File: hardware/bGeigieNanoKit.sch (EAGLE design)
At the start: 4 parts

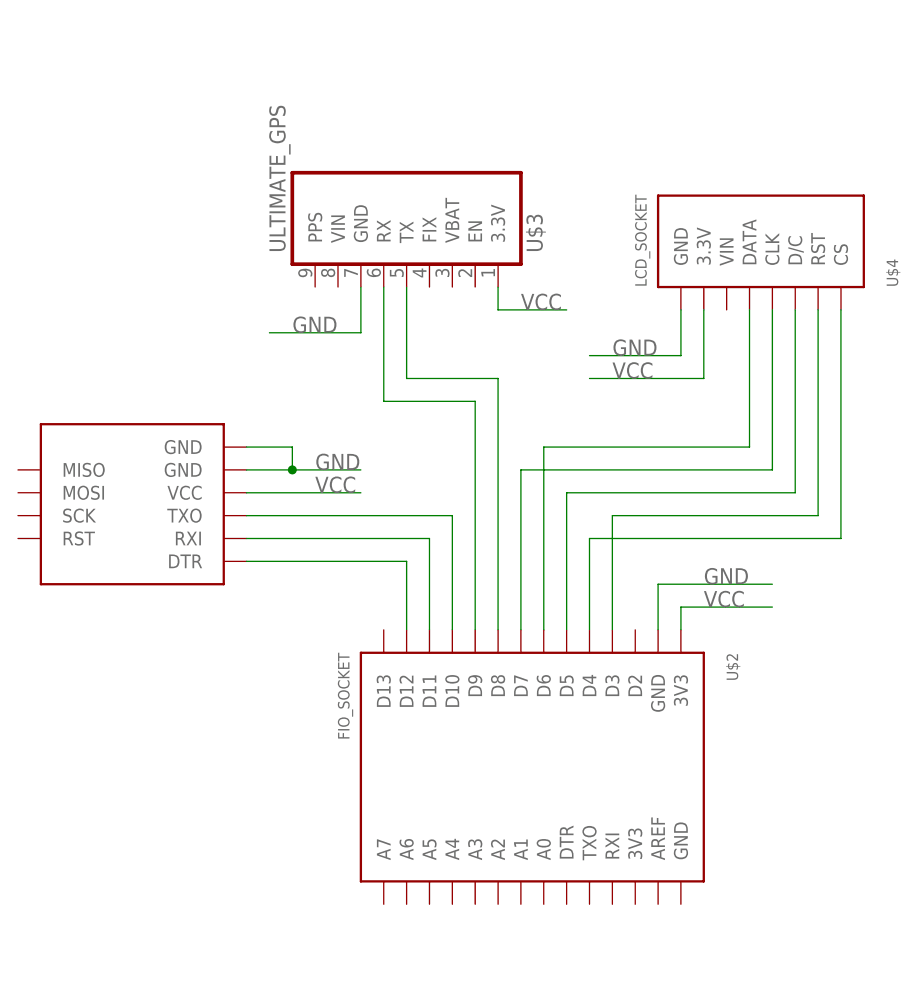
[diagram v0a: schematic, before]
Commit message: updated hardware files using auto generated footprints
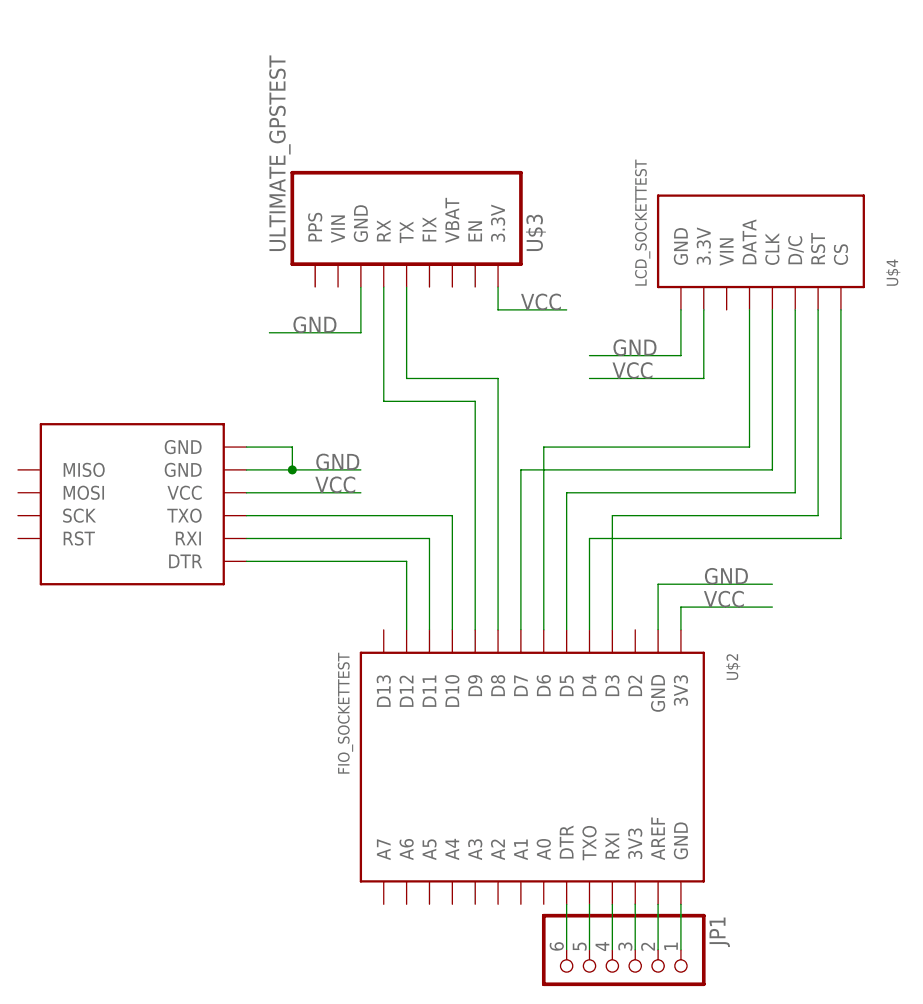
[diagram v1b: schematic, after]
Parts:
- added JP1: (no value), pinhead:PINHD-1X6
- U$1: value OPENLOG -> OPENLOGTEST; device open_hw_sockets:OPENLOG -> open_hw_sockets:OPENLOGTEST
- U$2: value FIO_SOCKET -> FIO_SOCKETTEST; device open_hw_sockets:FIO_SOCKET -> open_hw_sockets:FIO_SOCKETTEST
- U$3: value ULTIMATE_GPS -> ULTIMATE_GPSTEST; device open_hw_sockets:ULTIMATE_GPS -> open_hw_sockets:ULTIMATE_GPSTEST
- U$4: value LCD_SOCKET -> LCD_SOCKETTEST; device open_hw_sockets:LCD_SOCKET -> open_hw_sockets:LCD_SOCKETTEST
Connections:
- new net N$11: JP1.1, U$2.GND@2
- new net N$12: JP1.2, U$2.AREF
- new net N$13: JP1.3, U$2.3V3@2
- new net N$14: JP1.4, U$2.RXI
- new net N$15: JP1.5, U$2.TXO
- new net N$16: JP1.6, U$2.DTR
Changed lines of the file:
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@@
 <grid distance="0.1" unitdist="inch" unit="inch" style="lines" multiple="1" display="no" altdistance="0.01" altunitdist="inch" altunit="inch"/>
 <layers>
-<layer number="1" name="Top" color="4" fill="1" visible="no" active="no"/>
-<layer number="2" name="Route2" color="1" fill="3" visible="no" active="no"/>
-<layer number="3" name="Route3" color="4" fill="3" visible="no" active="no"/>
-<layer number="14" name="Route14" color="1" fill="6" visible="no" active="no"/>
-<layer number="15" name="Route15" color="4" fill="6" visible="no" active="no"/>
-<layer number="16" name="Bottom" color="1" fill="1" visible="no" active="no"/>
-<layer number="17" name="Pads" color="2" fill="1" visible="no" active="no"/>
-<layer number="18" name="Vias" color="2" fill="1" visible="no" active="no"/>
-<layer number="19" name="Unrouted" color="6" fill="1" visible="no" active="no"/>
-<layer number="20" name="Dimension" color="15" fill="1" visible="no" active="no"/>
-<layer number="21" name="tPlace" color="7" fill="1" visible="no" active="no"/>
-<layer number="22" name="bPlace" color="7" fill="1" visible="no" active="no"/>
-<layer number="23" name="tOrigins" color="15" fill="1" visible="no" active="no"/>
-<layer number="24" name="bOrigins" color="15" fill="1" visible="no" active="no"/>
-<layer number="25" name="tNames" color="7" fill="1" visible="no" active="no"/>
-<layer number="26" name="bNames" color="7" fill="1" visible="no" active="no"/>
-<layer number="27" name="tValues" color="7" fill="1" visible="no" active="no"/>
-<layer number="28" name="bValues" color="7" fill="1" visible="no" active="no"/>
+<layer number="1" name="Top" color="4" fill="1" visible="yes" active="no"/>
+<layer number="2" name="Route2" color="1" fill="3" visible="yes" active="no"/>
+<layer number="3" name="Route3" color="4" fill="3" visible="yes" active="no"/>
+<layer number="14" name="Route14" color="1" fill="6" visible="yes" active="no"/>
+<layer number="15" name="Route15" color="4" fill="6" visible="yes" active="no"/>
+<layer number="16" name="Bottom" color="1" fill="1" visible="yes" active="no"/>
+<layer number="17" name="Pads" color="2" fill="1" visible="yes" active="no"/>
+<layer number="18" name="Vias" color="2" fill="1" visible="yes" active="no"/>
+<layer number="19" name="Unrouted" color="6" fill="1" visible="yes" active="no"/>
+<layer number="20" name="Dimension" color="15" fill="1" visible="yes" active="no"/>
+<layer number="21" name="tPlace" color="7" fill="1" visible="yes" active="no"/>
+<layer number="22" name="bPlace" color="7" fill="1" visible="yes" active="no"/>
+<layer number="23" name="tOrigins" color="15" fill="1" visible="yes" active="no"/>
+<layer number="24" name="bOrigins" color="15" fill="1" visible="yes" active="no"/>
+<layer number="25" name="tNames" color="7" fill="1" visible="yes" active="no"/>
+<layer number="26" name="bNames" color="7" fill="1" visible="yes" active="no"/>
+<layer number="27" name="tValues" color="7" fill="1" visible="yes" active="no"/>
+<layer number="28" name="bValues" color="7" fill="1" visible="yes" active="no"/>
 <layer number="29" name="tStop" color="7" fill="3" visible="no" active="no"/>
 <layer number="30" name="bStop" color="7" fill="6" visible="no" active="no"/>
@@
 <layer number="35" name="tGlue" color="7" fill="4" visible="no" active="no"/>
 <layer number="36" name="bGlue" color="7" fill="5" visible="no" active="no"/>
-<layer number="37" name="tTest" color="7" fill="1" visible="no" active="no"/>
-<layer number="38" name="bTest" color="7" fill="1" visible="no" active="no"/>
+<layer number="37" name="tTest" color="7" fill="1" visible="yes" active="no"/>
+<layer number="38" name="bTest" color="7" fill="1" visible="yes" active="no"/>
 <layer number="39" name="tKeepout" color="4" fill="11" visible="no" active="no"/>
 <layer number="40" name="bKeepout" color="1" fill="11" visible="no" active="no"/>
@@
 <layer number="44" name="Drills" color="7" fill="1" visible="no" active="no"/>
 <layer number="45" name="Holes" color="7" fill="1" visible="no" active="no"/>
-<layer number="46" name="Milling" color="3" fill="1" visible="no" active="no"/>
-<layer number="47" name="Measures" color="7" fill="1" visible="no" active="no"/>
-<layer number="48" name="Document" color="7" fill="1" visible="no" active="no"/>
-<layer number="49" name="Reference" color="7" fill="1" visible="no" active="no"/>
-<layer number="50" name="dxf" color="7" fill="1" visible="no" active="no"/>
-<layer number="51" name="tDocu" color="7" fill="1" visible="no" active="no"/>
-<layer number="52" name="bDocu" color="7" fill="1" visible="no" active="no"/>
-<layer number="53" name="tGND_GNDA" color="7" fill="9" visible="no" active="no"/>
-<layer number="54" name="bGND_GNDA" color="1" fill="9" visible="no" active="no"/>
-<layer number="56" name="wert" color="7" fill="1" visible="no" active="no"/>
+<layer number="46" name="Milling" color="3" fill="1" visible="yes" active="no"/>
+<layer number="47" name="Measures" color="7" fill="1" visible="yes" active="no"/>
+<layer number="48" name="Document" color="7" fill="1" visible="yes" active="no"/>
+<layer number="49" name="Reference" color="7" fill="1" visible="yes" active="no"/>
+<layer number="50" name="dxf" color="7" fill="1" visible="yes" active="no"/>
+<layer number="51" name="tDocu" color="7" fill="1" visible="yes" active="no"/>
+<layer number="52" name="bDocu" color="7" fill="1" visible="yes" active="no"/>
+<layer number="53" name="tGND_GNDA" color="7" fill="9" visible="yes" active="no"/>
+<layer number="54" name="bGND_GNDA" color="1" fill="9" visible="yes" active="no"/>
+<layer number="56" name="wert" color="7" fill="1" visible="yes" active="no"/>
 <layer number="91" name="Nets" color="2" fill="1" visible="yes" active="yes"/>
 <layer number="92" name="Busses" color="1" fill="1" visible="yes" active="yes"/>
@@
 <parts>
 <part name="FRAME1" library="frames" deviceset="FRAME_A_L" device=""/>
-<part name="U$1" library="open_hw_sockets" deviceset="OPENLOG" device=""/>
-<part name="U$4" library="open_hw_sockets" deviceset="LCD_SOCKET" device=""/>
-<part name="U$3" library="open_hw_sockets" deviceset="ULTIMATE_GPS" device=""/>
-<part name="U$2" library="open_hw_sockets" deviceset="FIO_SOCKET" device=""/>
+<part name="U$1" library="open_hw_sockets" deviceset="OPENLOG" device="TEST" value="OPENLOGTEST"/>
+<part name="U$4" library="open_hw_sockets" deviceset="LCD_SOCKET" device="TEST" value="LCD_SOCKETTEST"/>
+<part name="U$3" library="open_hw_sockets" deviceset="ULTIMATE_GPS" device="TEST" value="ULTIMATE_GPSTEST"/>
+<part name="U$2" library="open_hw_sockets" deviceset="FIO_SOCKET" device="TEST" value="FIO_SOCKETTEST"/>
+<part name="JP1" library="pinhead" deviceset="PINHD-1X6" device=""/>
 </parts>
 <sheets>
@@
 <instance part="U$3" gate="G$1" x="119.38" y="149.86" rot="MR90"/>
 <instance part="U$2" gate="G$1" x="134.62" y="88.9" rot="R270"/>
+<instance part="JP1" gate="A" x="142.24" y="66.04" rot="R270"/>
 </instances>
 <busses>
@@
 </segment>
 </net>
+<net name="N$11" class="0">
+<segment>
+<pinref part="U$2" gate="G$1" pin="GND@2"/>
+<pinref part="JP1" gate="A" pin="1"/>
+<wire x1="149.86" y1="68.58" x2="149.86" y2="73.66" width="0.1524" layer="91"/>
+</segment>
+</net>
+<net name="N$12" class="0">
+<segment>
+<pinref part="U$2" gate="G$1" pin="AREF"/>
+<pinref part="JP1" gate="A" pin="2"/>
+<wire x1="147.32" y1="68.58" x2="147.32" y2="73.66" width="0.1524" layer="91"/>
+</segment>
+</net>
+<net name="N$13" class="0">
+<segment>
+<pinref part="U$2" gate="G$1" pin="3V3@2"/>
+<pinref part="JP1" gate="A" pin="3"/>
+<wire x1="144.78" y1="68.58" x2="144.78" y2="73.66" width="0.1524" layer="91"/>
+</segment>
+</net>
+<net name="N$14" class="0">
+<segment>
+<pinref part="U$2" gate="G$1" pin="RXI"/>
+<pinref part="JP1" gate="A" pin="4"/>
+<wire x1="142.24" y1="68.58" x2="142.24" y2="73.66" width="0.1524" layer="91"/>
+</segment>
+</net>
+<net name="N$15" class="0">
+<segment>
+<pinref part="U$2" gate="G$1" pin="TXO"/>
+<pinref part="JP1" gate="A" pin="5"/>
+<wire x1="139.7" y1="68.58" x2="139.7" y2="73.66" width="0.1524" layer="91"/>
+</segment>
+</net>
+<net name="N$16" class="0">
+<segment>
+<pinref part="U$2" gate="G$1" pin="DTR"/>
+<pinref part="JP1" gate="A" pin="6"/>
+<wire x1="137.16" y1="68.58" x2="137.16" y2="73.66" width="0.1524" layer="91"/>
+</segment>
+</net>
